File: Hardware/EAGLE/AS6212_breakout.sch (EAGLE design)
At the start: 19 parts, among them J2 QWIIC_RIGHT_ANGLE, J3 QWIIC_RIGHT_ANGLE, U1 AS6212

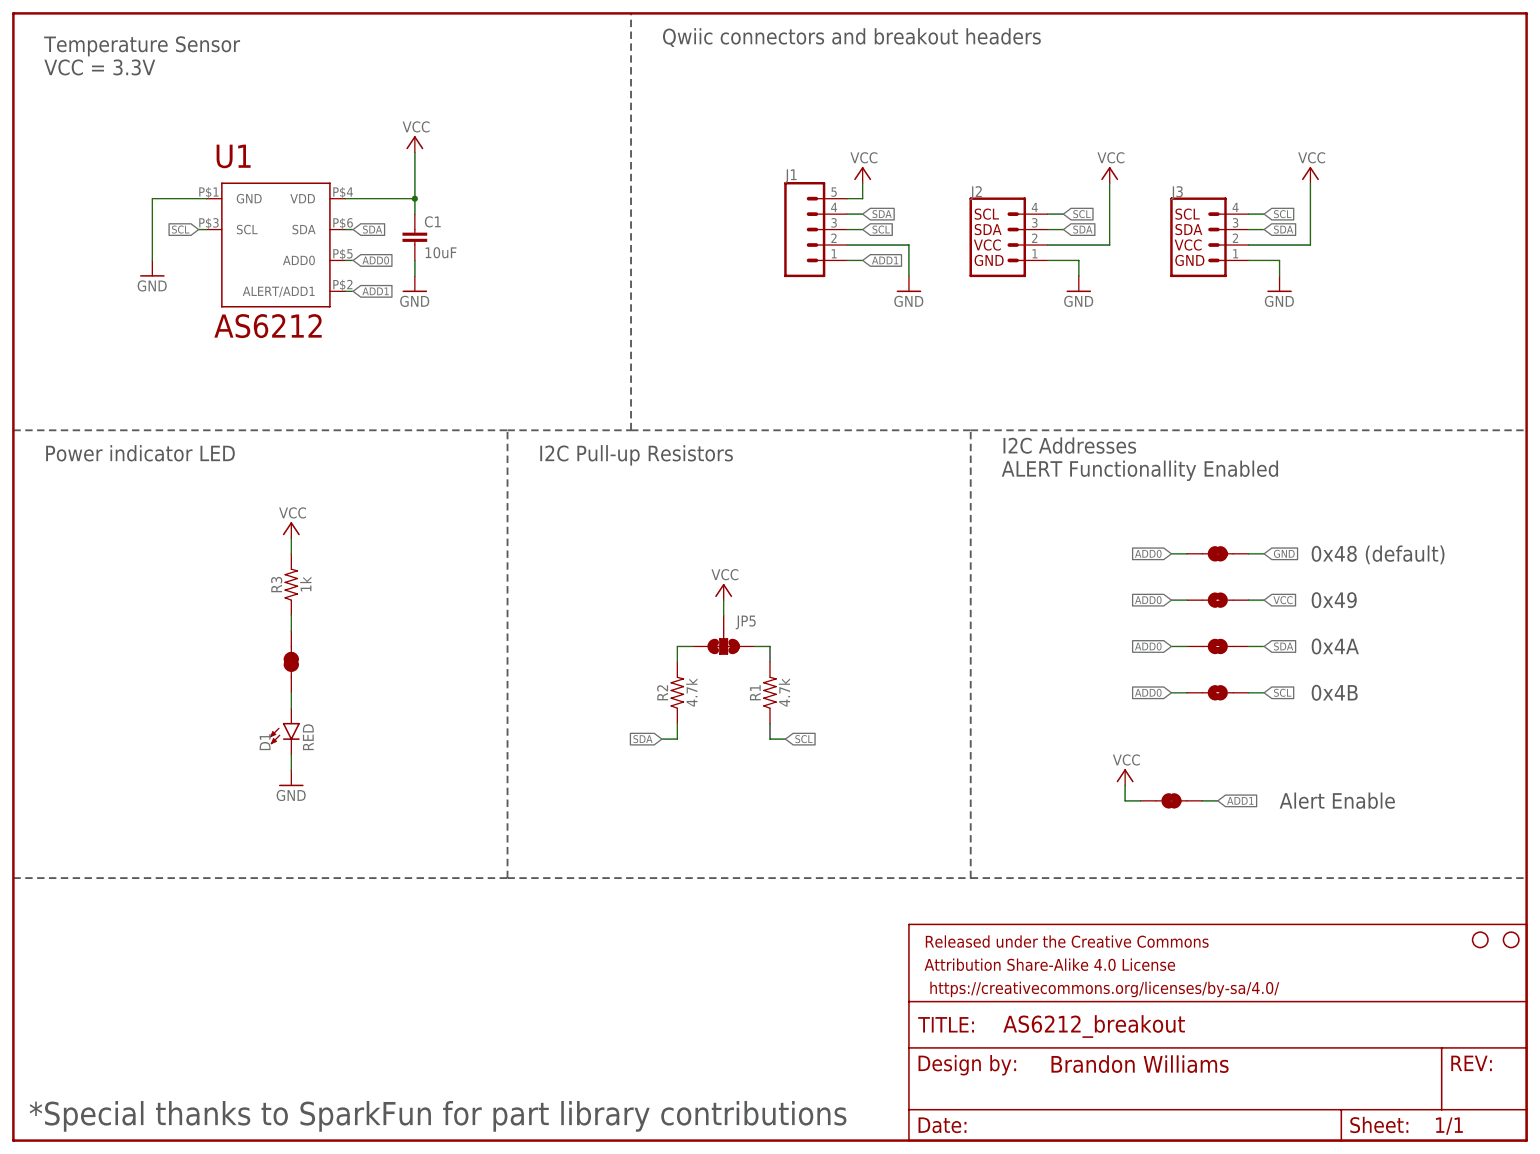
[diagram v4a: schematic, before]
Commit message: Board design rework & datasheet upload
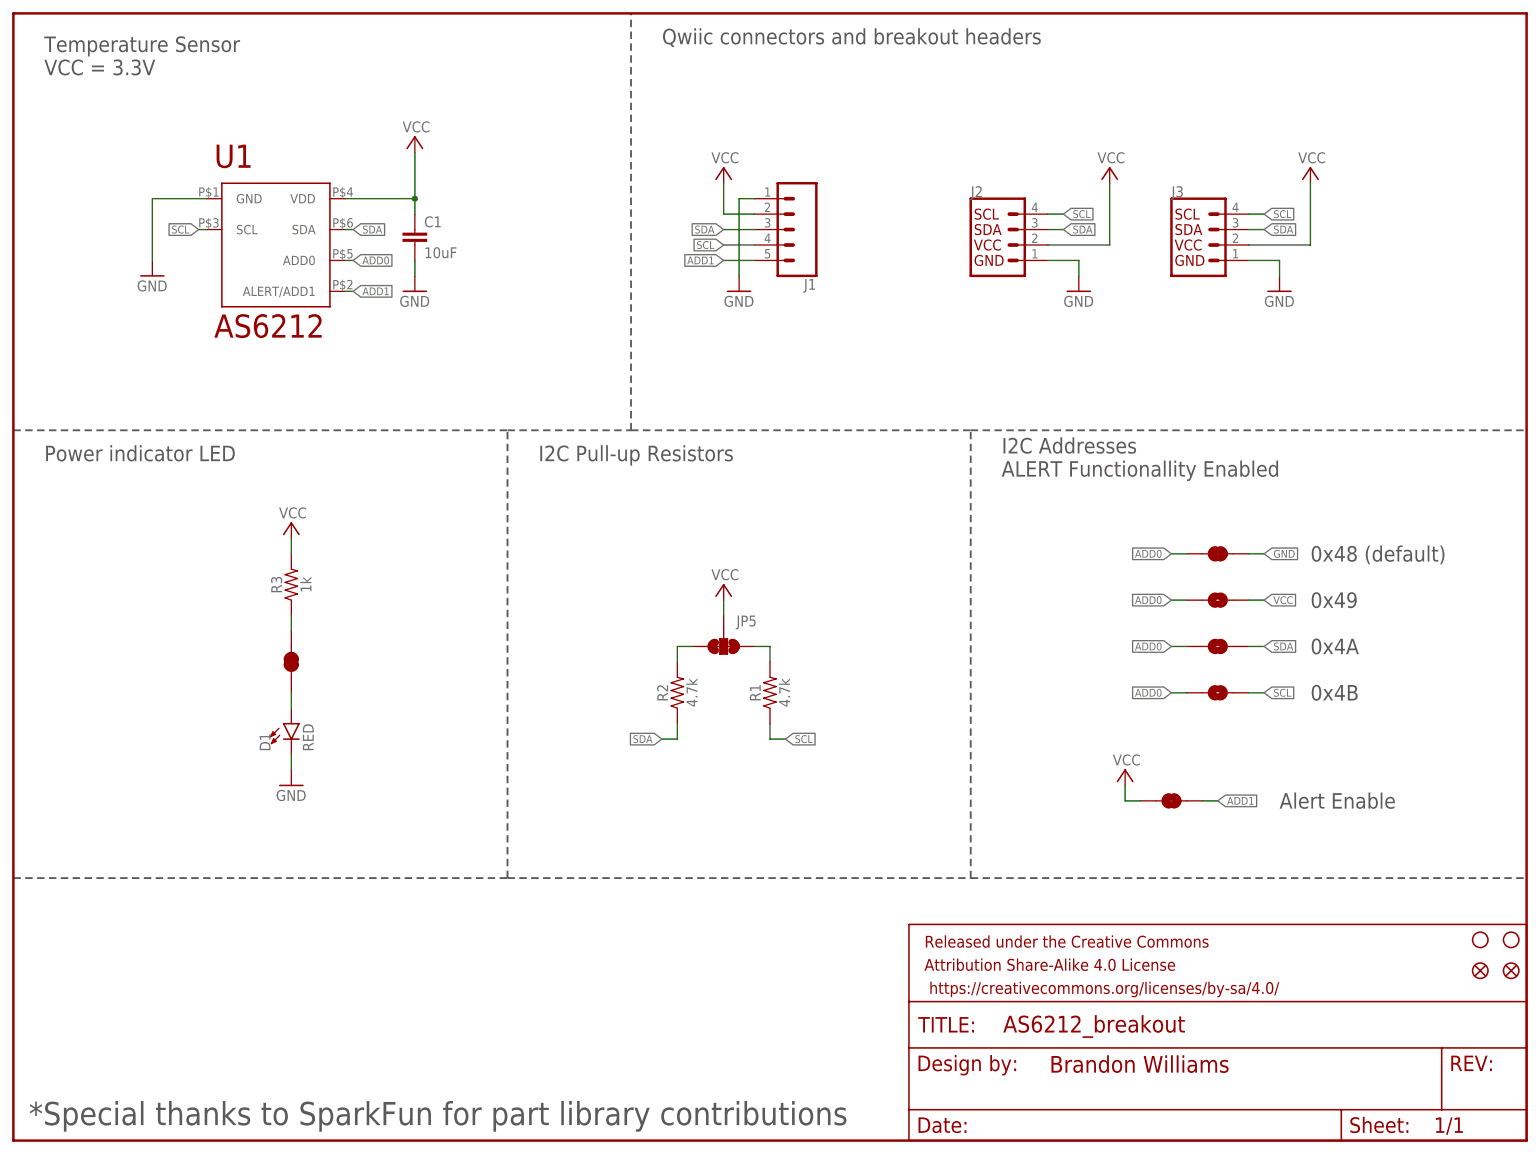
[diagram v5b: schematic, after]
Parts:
- added FD1, FD2: FIDUCIAL0.2MM, SparkFun-Aesthetics:FIDUCIAL0.2MM
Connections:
- net ADD1: now also J1.5; no longer J1.1
- net GND: now also J1.1; no longer J1.2
- net SCL: now also J1.4; no longer J1.3
- net SDA: now also J1.3; no longer J1.4
- net VCC: now also J1.2; no longer J1.5
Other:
- moved on the sheet: J1
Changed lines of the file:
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@@
 <layer number="128" name="_bValues" color="7" fill="1" visible="no" active="no"/>
 <layer number="129" name="Mask" color="7" fill="1" visible="no" active="no"/>
+<layer number="130" name="SMDSTROOK" color="7" fill="1" visible="no" active="no"/>
 <layer number="131" name="tAdjust" color="7" fill="1" visible="no" active="no"/>
 <layer number="132" name="bAdjust" color="7" fill="1" visible="no" active="no"/>
+<layer number="133" name="bottom_silk" color="7" fill="1" visible="no" active="no"/>
+<layer number="134" name="silk_top" color="7" fill="1" visible="no" active="no"/>
+<layer number="135" name="silk_bottom" color="7" fill="1" visible="no" active="no"/>
+<layer number="136" name="silktop" color="7" fill="1" visible="no" active="no"/>
+<layer number="137" name="silkbottom" color="7" fill="1" visible="no" active="no"/>
+<layer number="138" name="EEE" color="7" fill="1" visible="no" active="no"/>
+<layer number="139" name="_tKeepout" color="7" fill="1" visible="no" active="no"/>
+<layer number="140" name="mbKeepout" color="7" fill="1" visible="no" active="no"/>
+<layer number="141" name="ASSEMBLY_TOP" color="7" fill="1" visible="no" active="no"/>
+<layer number="142" name="mbRestrict" color="7" fill="1" visible="no" active="no"/>
+<layer number="143" name="PLACE_BOUND_TOP" color="7" fill="1" visible="no" active="no"/>
 <layer number="144" name="Drill_legend" color="7" fill="1" visible="no" active="no"/>
+<layer number="145" name="DrillLegend_01-16" color="7" fill="1" visible="no" active="no"/>
+<layer number="146" name="DrillLegend_01-20" color="7" fill="1" visible="no" active="no"/>
+<layer number="147" name="PIN_NUMBER" color="7" fill="1" visible="no" active="no"/>
+<layer number="149" name="DrillLegend_02-15" color="7" fill="1" visible="no" active="no"/>
 <layer number="150" name="Notes" color="7" fill="1" visible="no" active="no"/>
 <layer number="151" name="HeatSink" color="7" fill="1" visible="no" active="no"/>
@@
 <layer number="154" name="FabDoc2" color="7" fill="1" visible="no" active="no"/>
 <layer number="155" name="FabDoc3" color="7" fill="1" visible="no" active="no"/>
+<layer number="166" name="AntennaArea" color="7" fill="1" visible="no" active="no"/>
+<layer number="168" name="4mmHeightArea" color="7" fill="1" visible="no" active="no"/>
+<layer number="191" name="mNets" color="7" fill="1" visible="no" active="no"/>
+<layer number="192" name="mBusses" color="7" fill="1" visible="no" active="no"/>
+<layer number="193" name="mPins" color="7" fill="1" visible="no" active="no"/>
+<layer number="194" name="mSymbols" color="7" fill="1" visible="no" active="no"/>
+<layer number="195" name="mNames" color="7" fill="1" visible="no" active="no"/>
+<layer number="196" name="mValues" color="7" fill="1" visible="no" active="no"/>
 <layer number="199" name="Contour" color="7" fill="1" visible="no" active="no"/>
 <layer number="200" name="200bmp" color="1" fill="10" visible="no" active="no"/>
@@
 <part name="JP7" library="SparkFun-Jumpers" deviceset="JUMPER-SMT_2_NC_TRACE" device="_SILK" package3d_urn="urn:adsk.eagle:package:39281/1"/>
 <part name="GND3" library="supply1" library_urn="urn:adsk.eagle:library:371" deviceset="GND" device=""/>
+<part name="FD1" library="SparkFun-Aesthetics" deviceset="FIDUCIAL" device="0.2MM"/>
+<part name="FD2" library="SparkFun-Aesthetics" deviceset="FIDUCIAL" device="0.2MM"/>
 </parts>
 <sheets>
@@
 <instance part="JP3" gate="G$1" x="198.12" y="88.9" smashed="yes"/>
 <instance part="JP4" gate="G$1" x="198.12" y="96.52" smashed="yes"/>
-<instance part="J1" gate="G$1" x="129.54" y="149.86" smashed="yes">
-<attribute name="VALUE" x="127" y="139.954" size="1.778" layer="96" font="vector"/>
-<attribute name="NAME" x="127" y="157.988" size="1.778" layer="95" font="vector"/>
+<instance part="J1" gate="G$1" x="129.54" y="149.86" smashed="yes" rot="R180">
+<attribute name="VALUE" x="132.08" y="159.766" size="1.778" layer="96" font="vector" rot="R180"/>
+<attribute name="NAME" x="132.08" y="141.732" size="1.778" layer="95" font="vector" rot="R180"/>
 </instance>
 <instance part="GND2" gate="1" x="66.04" y="139.7" smashed="yes">
@@
 <attribute name="VALUE" x="119.38" y="93.98" size="1.778" layer="96" rot="R180"/>
 </instance>
-<instance part="P+3" gate="VCC" x="139.7" y="160.02" smashed="yes">
-<attribute name="VALUE" x="142.24" y="162.56" size="1.778" layer="96" rot="R180"/>
+<instance part="P+3" gate="VCC" x="116.84" y="160.02" smashed="yes">
+<attribute name="VALUE" x="119.38" y="162.56" size="1.778" layer="96" rot="R180"/>
 </instance>
 <instance part="P+4" gate="VCC" x="180.34" y="160.02" smashed="yes">
@@
 </instance>
 <instance part="JP7" gate="G$1" x="45.72" y="78.74" smashed="yes" rot="R90"/>
-<instance part="GND3" gate="1" x="147.32" y="139.7" smashed="yes">
-<attribute name="VALUE" x="144.78" y="137.16" size="1.778" layer="96"/>
-</instance>
+<instance part="GND3" gate="1" x="119.38" y="139.7" smashed="yes">
+<attribute name="VALUE" x="116.84" y="137.16" size="1.778" layer="96"/>
+</instance>
+<instance part="FD1" gate="G$1" x="241.3" y="27.94" smashed="yes"/>
+<instance part="FD2" gate="G$1" x="246.38" y="27.94" smashed="yes"/>
 </instances>
 <busses>
@@
 </segment>
 <segment>
-<pinref part="J1" gate="G$1" pin="5"/>
-<wire x1="137.16" y1="154.94" x2="139.7" y2="154.94" width="0.1524" layer="91"/>
-<wire x1="139.7" y1="154.94" x2="139.7" y2="157.48" width="0.1524" layer="91"/>
-<pinref part="P+3" gate="VCC" pin="VCC"/>
-</segment>
-<segment>
 <pinref part="J2" gate="G$1" pin="2"/>
 <wire x1="170.18" y1="147.32" x2="180.34" y2="147.32" width="0.1524" layer="91"/>
@@
 <wire x1="45.72" y1="99.06" x2="45.72" y2="96.52" width="0.1524" layer="91"/>
 </segment>
+<segment>
+<pinref part="P+3" gate="VCC" pin="VCC"/>
+<pinref part="J1" gate="G$1" pin="2"/>
+<wire x1="116.84" y1="157.48" x2="116.84" y2="152.4" width="0.1524" layer="91"/>
+<wire x1="116.84" y1="152.4" x2="121.92" y2="152.4" width="0.1524" layer="91"/>
+</segment>
 </net>
 <net name="ADD0" class="0">
@@
 </segment>
 <segment>
-<pinref part="J1" gate="G$1" pin="4"/>
-<wire x1="137.16" y1="152.4" x2="139.7" y2="152.4" width="0.1524" layer="91"/>
-<label x="139.7" y="152.4" size="1.27" layer="95" xref="yes"/>
-</segment>
-<segment>
 <pinref part="J2" gate="G$1" pin="3"/>
 <wire x1="170.18" y1="149.86" x2="172.72" y2="149.86" width="0.1524" layer="91"/>
@@
 <wire x1="203.2" y1="149.86" x2="205.74" y2="149.86" width="0.1524" layer="91"/>
 <label x="205.74" y="149.86" size="1.27" layer="95" xref="yes"/>
+</segment>
+<segment>
+<pinref part="J1" gate="G$1" pin="3"/>
+<wire x1="121.92" y1="149.86" x2="116.84" y2="149.86" width="0.1524" layer="91"/>
+<label x="116.84" y="149.86" size="1.27" layer="95" rot="R180" xref="yes"/>
 </segment>
 </net>
@@
 </segment>
 <segment>
-<pinref part="J1" gate="G$1" pin="3"/>
-<wire x1="137.16" y1="149.86" x2="139.7" y2="149.86" width="0.1524" layer="91"/>
-<label x="139.7" y="149.86" size="1.27" layer="95" xref="yes"/>
-</segment>
-<segment>
 <pinref part="J2" gate="G$1" pin="4"/>
 <wire x1="170.18" y1="152.4" x2="172.72" y2="152.4" width="0.1524" layer="91"/>
@@
 <wire x1="203.2" y1="152.4" x2="205.74" y2="152.4" width="0.1524" layer="91"/>
 <label x="205.74" y="152.4" size="1.27" layer="95" xref="yes"/>
+</segment>
+<segment>
+<pinref part="J1" gate="G$1" pin="4"/>
+<wire x1="121.92" y1="147.32" x2="116.84" y2="147.32" width="0.1524" layer="91"/>
+<label x="116.84" y="147.32" size="1.27" layer="95" rot="R180" xref="yes"/>
 </segment>
 </net>
@@
 </segment>
 <segment>
-<pinref part="J1" gate="G$1" pin="2"/>
+<pinref part="J1" gate="G$1" pin="1"/>
 <pinref part="GND3" gate="1" pin="GND"/>
-<wire x1="137.16" y1="147.32" x2="147.32" y2="147.32" width="0.1524" layer="91"/>
-<wire x1="147.32" y1="147.32" x2="147.32" y2="142.24" width="0.1524" layer="91"/>
+<wire x1="121.92" y1="154.94" x2="119.38" y2="154.94" width="0.1524" layer="91"/>
+<wire x1="119.38" y1="154.94" x2="119.38" y2="142.24" width="0.1524" layer="91"/>
 </segment>
 </net>
@@
 </segment>
 <segment>
-<pinref part="J1" gate="G$1" pin="1"/>
-<wire x1="137.16" y1="144.78" x2="139.7" y2="144.78" width="0.1524" layer="91"/>
-<label x="139.7" y="144.78" size="1.27" layer="95" xref="yes"/>
-</segment>
-</net>
+<pinref part="J1" gate="G$1" pin="5"/>
+<wire x1="121.92" y1="144.78" x2="116.84" y2="144.78" width="0.1524" layer="91"/>
+<label x="116.84" y="144.78" size="1.27" layer="95" rot="R180" xref="yes"/>
+</segment>
+</net>
